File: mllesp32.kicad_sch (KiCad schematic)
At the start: 66 parts, among them IC1 LM393, J1 Conn_02x03_Odd_Even, J2 Conn_02x03_Odd_Even, J3 Conn_02x03_Odd_Even, J4 Conn_02x03_Odd_Even, J5 Conn_02x03_Odd_Even, J6 Conn_02x03_Odd_Even, J7 Conn_02x03_Odd_Even, J8 Conn_02x03_Odd_Even, J9 Screw_Terminal_01x03, Q1 BC547, U1 6N137, U2 ESP32-DEVKITC-32D, U3 CRE1S0505S3C, U4 ISO1050DUB, U5 L7805

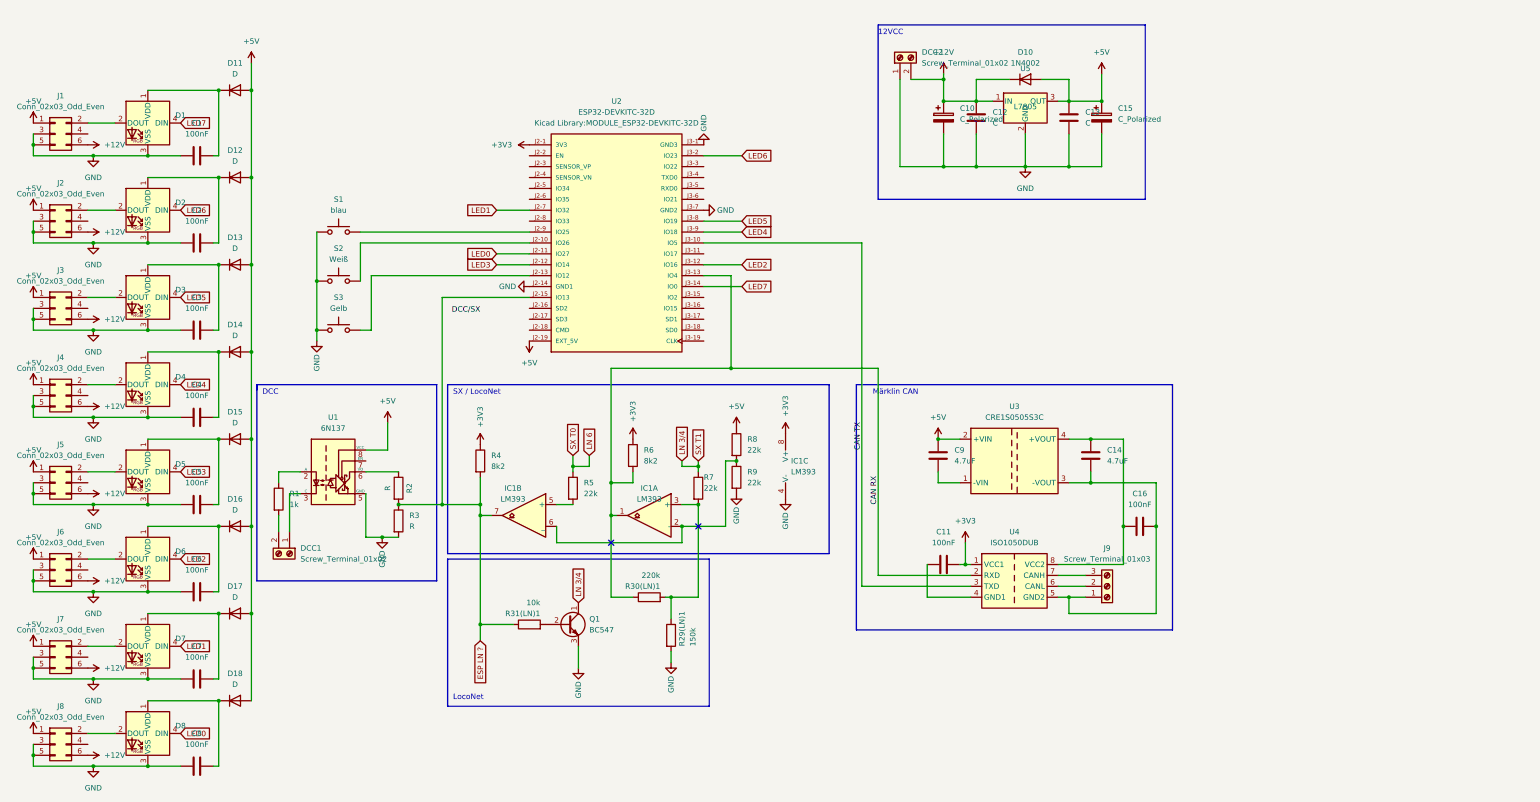
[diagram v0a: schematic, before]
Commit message: First Draft
Level Shift Missing
SX/LN incomplete
Output Jacks missing
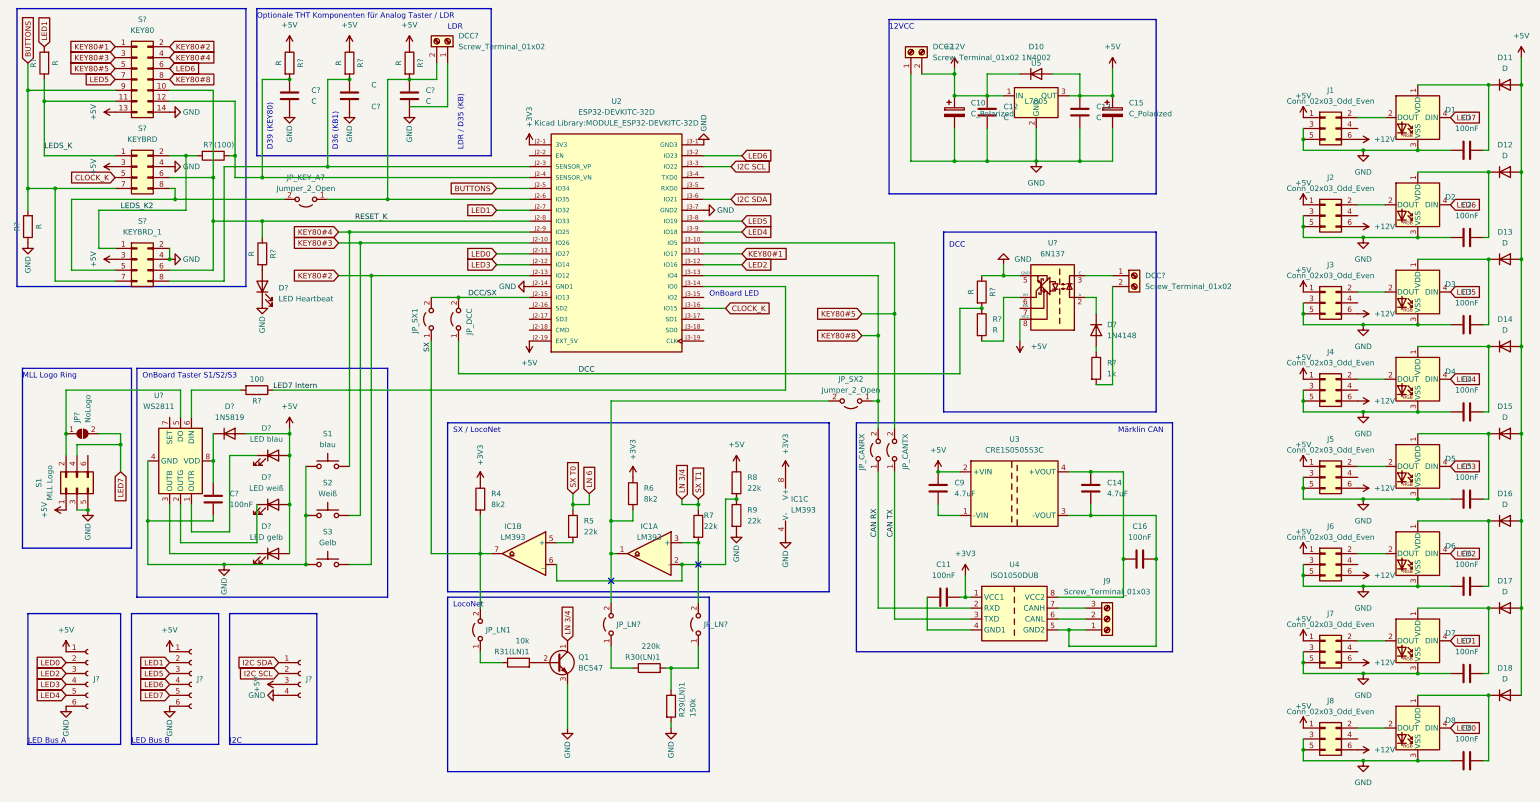
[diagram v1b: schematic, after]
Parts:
- removed DCC1: Screw_Terminal_01x02, Connector_PinHeader_2.54mm:PinHeader_1x02_P2.54mm_Horizontal, symbol Connector:Screw_Terminal_01x02
- removed R1: 1k, Resistor_THT:R_Axial_DIN0207_L6.3mm_D2.5mm_P15.24mm_Horizontal, symbol Device:R
- removed R2, R3: R, Resistor_THT:R_Axial_DIN0207_L6.3mm_D2.5mm_P15.24mm_Horizontal, symbol Device:R
- removed U1: 6N137, Package_DIP:DIP-8_W7.62mm, symbol Isolator:6N137
- added C? (x3): C, Capacitor_SMD:C_0805_2012Metric_Pad1.18x1.45mm_HandSolder, symbol Device:C
- added C?: 100nF, Capacitor_SMD:C_0805_2012Metric_Pad1.18x1.45mm_HandSolder, symbol Device:C
- added D?: LED blau, symbol Device:LED
- added D?: LED Heartbeat, symbol Device:LED
- added D?: 1N5819, Diode_SMD:D_0805_2012Metric_Pad1.15x1.40mm_HandSolder, symbol Device:D
- added D?: 1N4148, Diode_THT:D_DO-41_SOD81_P10.16mm_Horizontal, symbol Diode:1N4002
- added D?: LED weiß, symbol Device:LED
- added D?: LED gelb, symbol Device:LED
- added DCC? (x2): Screw_Terminal_01x02, Connector_PinHeader_2.54mm:PinHeader_1x02_P2.54mm_Horizontal, symbol Connector:Screw_Terminal_01x02
- added J? (x2): Conn_01x06_Female, symbol Connector:Conn_01x06_Female
- added J?: Conn_01x04_Female, symbol Connector:Conn_01x04_Female
- added JP?: NoLogo, symbol Jumper:SolderJumper_2_Open
- added JP_CANRX, JP_CANTX, JP_DCC, JP_KEY_A7, JP_LN1, JP_LN? (x2), JP_SX1, JP_SX2: Jumper_2_Open, symbol Jumper:Jumper_2_Open
- added R? (x7): R, Resistor_THT:R_Axial_DIN0207_L6.3mm_D2.5mm_P15.24mm_Horizontal, symbol Device:R
- added R?: 1k, Resistor_THT:R_Axial_DIN0207_L6.3mm_D2.5mm_P15.24mm_Horizontal, symbol Device:R
- added R?: (100), Resistor_THT:R_Axial_DIN0207_L6.3mm_D2.5mm_P15.24mm_Horizontal, symbol Device:R
- added R?: R, Resistor_SMD:R_1206_3216Metric_Pad1.30x1.75mm_HandSolder, symbol Device:R
- added R?: 100, Resistor_THT:R_Axial_DIN0207_L6.3mm_D2.5mm_P15.24mm_Horizontal, symbol Device:R
- added S1: MLL Logo, Connector_IDC:IDC-Header_2x03_P2.54mm_Vertical, symbol Connector_Generic:Conn_02x03_Odd_Even
- added S?: KEYBRD, Connector_IDC:IDC-Header_2x04_P2.54mm_Vertical, symbol Connector_Generic:Conn_02x04_Odd_Even
- added S?: KEYBRD_1, Connector_IDC:IDC-Header_2x04_P2.54mm_Vertical, symbol Connector_Generic:Conn_02x04_Odd_Even
- added S?: KEY80, Connector_IDC:IDC-Header_2x04_P2.54mm_Vertical, symbol Connector_Generic:Conn_02x07_Odd_Even
- added U?: WS2811, symbol Driver_LED:WS2811
- added U?: 6N137, Package_DIP:DIP-8_W7.62mm, symbol Isolator:6N137
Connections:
- net +5V: now also D?.2 (A), D?.2 (A), D?.2 (A), D?.2 (A), J?.1 (Pin_1), J?.1 (Pin_1), J?.3 (Pin_3), R?.1, R?.1, R?.1, S1.1 (Pin_1), S?.13 (Pin_13), S?.3 (Pin_3), S?.3 (Pin_3), U?.8 (VCC)
- net CAN RX: now also JP_CANRX.1 (A); no longer IC1.1, R30(LN)1.1, R6.2, U2.J3-13 (IO4)
- net CAN TX: now also JP_CANTX.1 (A); no longer U2.J3-10 (IO5)
- net DCC/SX: now also U2.J2-15 (IO13), JP_DCC.2 (B), JP_SX1.2 (B)
- net GND: now also C?.2, C?.2, C?.2, C?.2, D?.1 (K), J?.4 (Pin_4), J?.6 (Pin_6), J?.6 (Pin_6), R?.1, R?.1, S1.3 (Pin_3), S1.5 (Pin_5), S?.14 (Pin_14), S?.2 (Pin_2), S?.4 (Pin_4), S?.4 (Pin_4), U?.4 (GND), U?.5 (GND)
- net LED0: now also J?.2 (Pin_2)
- net LED1: now also J?.2 (Pin_2), R?.2
- net LED2: now also J?.3 (Pin_3)
- net LED3: now also J?.4 (Pin_4)
- net LED4: now also J?.5 (Pin_5)
- net LED5: now also J?.3 (Pin_3), S?.7 (Pin_7)
- net LED6: now also J?.4 (Pin_4), S?.6 (Pin_6)
- net LED7: now also J?.5 (Pin_5), JP?.2 (B), S1.4 (Pin_4); no longer U2.J3-14 (IO0)
- net at IC1.3 (+), R7.2: now also JP_LN?.2 (B); no longer R29(LN)1.1, R30(LN)1.2
- net KEY80#2: now reaches S3.2, U2.J2-13 (IO12)
- net KEY80#2: now also S?.2 (Pin_2)
- net KEY80#3: now reaches S2.2, U2.J2-10 (IO26)
- net KEY80#3: now also S?.3 (Pin_3)
- net at U2.J2-3 (SENSOR_VP): now also C?.1, R?.2, S?.8 (Pin_8)
- net at U2.J2-4 (SENSOR_VN): now also C?.1, R?.1, R?.2, S?.12 (Pin_12)
- net BUTTONS: now reaches U2.J2-5 (IO34)
- net BUTTONS: now also R?.2, S?.7 (Pin_7), S?.7 (Pin_7), S?.9 (Pin_9)
- net at U2.J2-6 (IO35): now also C?.1, DCC?.2 (Pin_2), JP_KEY_A7.1 (A), R?.2
- net RESET_K: now reaches U2.J2-8 (IO33)
- net RESET_K: now also R?.1, S?.10 (Pin_10), S?.6 (Pin_6), S?.6 (Pin_6)
- net KEY80#4: now reaches S1.2, U2.J2-9 (IO25)
- net KEY80#4: now also S?.4 (Pin_4)
- net KEY80#1: now reaches U2.J3-11 (IO17)
- net KEY80#1: now also S?.1 (Pin_1)
- net CLOCK_K: now reaches U2.J3-16 (IO15)
- net CLOCK_K: now also S?.5 (Pin_5)
- net I2C SCL: now reaches U2.J3-3 (IO22)
- net I2C SCL: now also J?.2 (Pin_2)
- net I2C SDA: now reaches U2.J3-6 (IO21)
- net I2C SDA: now also J?.1 (Pin_1)
- net ESP LN ?  renamed SX
- net SX: now also JP_LN1.2 (B), JP_SX1.1 (A); no longer R31(LN)1.1, U2.J2-15 (IO13)
- new net: D?.1 (K), U?.1 (OUTR)
- new net: D?.1 (K), U?.2 (OUTG)
- new net: D?.1 (K), U?.3 (OUTB)
- new net: JP?.1 (A), S1.2 (Pin_2), U?.5 (DO)
- new net: R?.2, U?.6 (DIN)
- new net: C?.1, D?.1 (K), U?.8 (VDD)
- new net: IC1.1, JP_LN?.2 (B), JP_SX2.2 (B), R6.2
- new net: D?.2 (A), R?.1
- new net: DCC?.2 (Pin_2), R?.2
- new net: JP_LN1.1 (A), R31(LN)1.1
- new net: D?.2 (A), R?.2
- new net: JP_KEY_A7.2 (B), S?.5 (Pin_5), S?.8 (Pin_8)
- new net: JP_LN?.1 (A), R30(LN)1.1
- new net: JP_LN?.1 (A), R29(LN)1.1, R30(LN)1.2
- new net: DCC?.1 (Pin_1), U?.3 (C)
- new net: R?.2, U?.6 (VO)
- new net: D?.1 (K), U?.2 (A)
- new net DCC: JP_DCC.1 (A), R?.1, R?.2
- new net KEY80#5: JP_CANTX.2 (B), S?.5 (Pin_5), U2.J3-10 (IO5)
- new net KEY80#8: JP_CANRX.2 (B), JP_SX2.1 (A), S?.8 (Pin_8), U2.J3-13 (IO4)
- new net LED7 Intern: R?.1, U2.J3-14 (IO0)
- new net LEDS_K: R?.1, S?.1 (Pin_1), S?.11 (Pin_11)
- new net LEDS_K2: R?.2, S?.1 (Pin_1), S?.2 (Pin_2)
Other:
- note added: "D36 (KB1)"
- note added: "D39 (KEY80)"
- note added: "I2C"
- note added: "LDR"
- note added: "LDR / D35 (KB)"
- note added: "LED Bus A"
- note added: "LED Bus B"
- note added: "MLL Logo Ring"
- note added: "OnBoard LED"
- note added: "OnBoard Taster S1/S2/S3"
- note added: "Optionale THT Komponenten für Analog Taster / LDR"
- moved on the sheet: C1, C10, C11, C12, C13, C14, C15, C16, C2, C3, C4, C5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
